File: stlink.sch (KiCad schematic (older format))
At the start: 7 parts, among them U5 STM32F103C(8-B)Tx

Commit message: Continue work at jtag
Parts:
- added C? (x2): 20pF/50V, symbol Capacitors_Smd0603:20pF
- added C?: 100n/50V, symbol Capacitors_Smd0603:100n
- added R? (x2): 10k, symbol Resistors_Smd0603:10k
- added R? (x2): 4k7, symbol Resistors_Smd0603:4k7
- added R?: 100k, symbol Resistors_Smd0603:100k
- added U?: MCP1700T-3302E_MB, symbol Linear_Regulators:MCP1700T-3302E_MB
- added X?: 8.000MHZ, symbol Resonators:ABM3AIG-8.000MHZ-8-1R-T
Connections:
- net GND: now also C?.1, C?.1, C?.2, R?.1, R?.2, R?.2
- net at U5.10 (PA0-WKUP/ADC1_IN0/ADC2_IN0/SYS_WKUP/TIM2_CH1/TIM2_ETR/USART2_CTS): now also R?.2, R?.2
- net at U5.2 (PC13-TAMPER-RTC/RTC_OUT/RTC_TAMPER): now also R?.1
- net at U5.3 (PC14-OSC32_IN/RCC_OSC32_IN): now also R?.1
- net at U5.5 (PD0-OSC_IN/RCC_OSC_IN): now also C?.2, X?.1
- net at U5.6 (PD1-OSC_OUT/RCC_OSC_OUT): now also C?.2, X?.2
- net at U5.7 (NRST): now also C?.1, R?.2
- new net 3V3: R?.1, R?.1
- no-connect marks 0 -> 3

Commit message: Finished work at st-link, figurated elements on pcb
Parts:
- added C26: 1nF/2kV, Capacitors_Smd_1206:1nF_2kV_1206, symbol Capacitors_Smd1206:1nF_2kV_1206
- added C28, C29: 100nF/50V, Capacitors_Smd_0603:100nF_0603, symbol Capacitors_Smd0603:100nF_0603
- added C30: 10uF/6V3, Capacitors_Smd_0805:10uF_0805, symbol Capacitors_Smd0805:10uF_6V3
- added Con4: USB_C_Wurth_632723130112, Connector_USB:USB_C_632723130112, symbol USB_Connectors:USB_C_Wurth_632723130112
- added D2: BAT54C, Diodes:BAT54C, symbol Diodes:BAT54C
- added D3: HSMF-C155, Diodes:HSMF-C155, symbol Diodes:HSMF-C155
- added Q1: BC847B, Transistor_Bipolar:BC847B_SOT23, symbol Transistor_Bipolar:BC847B
- added R10: 10k, Resistor_Smd_0603:10k_0603, symbol Resistors_Smd0603:10k
- added R11: 36k, Resistor_Smd_0603:36k_0603, symbol Resistors_Smd0603:36k
- added R12, R15: 22R, Resistor_Smd_0603:22R_0603, symbol Resistors_Smd0603:22R
- added R13: 1k5, Resistor_Smd_0603:1k5_0603, symbol Resistors_Smd0603:1k5
- added R14, R23: 100R, Resistor_Smd_0603:100R_0603, symbol Resistors_Smd0603:100R
- added R16, R17: 220R, Resistor_Smd_0603:220R_0603, symbol Resistors_Smd0603:220R
- added R21: 100k, Resistor_Smd_0603:100k_0603, symbol Resistors_Smd0603:100k
- added R24: 0R, Resistor_Smd_0603:0R_0603, symbol Resistors_Smd0603:0R
- C27: renamed from C?; footprint (none) -> Capacitors_Smd_0603:100nF_0603
- C31, C32: renamed from C?; footprint (none) -> Capacitors_Smd_0603:20pF_0603
- R18, R20: renamed from R?; footprint (none) -> Resistor_Smd_0603:10k_0603
- R19, R22: renamed from R?; footprint (none) -> Resistor_Smd_0603:4k7_0603
- R9: renamed from R?; footprint (none) -> Resistor_Smd_0603:100k_0603
- U6: renamed from U?; footprint (none) -> Linear:MCP1700T-3302E_MB_SOT89
- X1: renamed from X?; footprint (none) -> Resonators:ABM3AIG-8.000MHZ-8-1R-T
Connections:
- net 3V3: now also C21.1, C22.1, C23.1, C24.1, C25.1, L6.2, U5.1 (VBAT), U5.24 (VDD), U5.36 (VDD), U5.48 (VDD), U6.3 (Vout), C29.1, C30.1, D3.1 (A1), Q1.3 (C)
- net GND: now also U5.20 (PB2), U6.1 (GND), C26.1, C28.2, C29.2, C30.2, Con4.A1 (GND), Con4.A12 (GND_1), Con4.B1 (GND_2), Con4.B12 (GND_3), D3.4 (C2), R11.1, R21.1, R24.1
- net STLINK_TX: now reaches U5.12 (PA2/ADC1_IN2/ADC2_IN2/TIM2_CH3/USART2_TX)
- net STLINK_RX: now reaches U5.13 (PA3/ADC1_IN3/ADC2_IN3/TIM2_CH4/USART2_RX)
- net JTCK: now reaches U5.15 (PA5/ADC1_IN5/ADC2_IN5/SPI1_SCK)
- net JTDO: now reaches U5.16 (PA6/ADC1_IN6/ADC2_IN6/SPI1_MISO/TIM1_BKIN/TIM3_CH1)
- net JTDI: now reaches U5.17 (PA7/ADC1_IN7/ADC2_IN7/SPI1_MOSI/TIM1_CH1N/TIM3_CH2)
- net JTRST: now reaches U5.18 (PB0/ADC1_IN8/ADC2_IN8/TIM1_CH2N/TIM3_CH3)
- net at U5.25 (PB12/I2C2_SMBA/SPI2_NSS/TIM1_BKIN/USART3_CK): now also R23.2
- net STLINK-SWCLK: now reaches U5.26 (PB13/SPI2_SCK/TIM1_CH1N/USART3_CTS)
- net JTMS: now reaches U5.27 (PB14/SPI2_MISO/TIM1_CH2N/USART3_RTS)
- net JTMS: now also R23.1
- net at U5.30 (PA9/TIM1_CH2/USART1_TX): now also R16.2, R17.2
- net STLINK-SWO: now reaches U5.31 (PA10/TIM1_CH3/USART1_RX)
- net at U5.32 (PA11/ADC1_EXTI11/ADC2_EXTI11/CAN_RX/TIM1_CH4/USART1_CTS/USB_DM): now also R12.1
- net at U5.33 (PA12/CAN_TX/TIM1_ETR/USART1_RTS/USB_DP): now also R15.1
- net STM-JTMS-SWDIO: now reaches U5.34 (PA13/SYS_JTMS-SWDIO)
- net STM-JTCK-SWCLK: now reaches U5.37 (PA14/SYS_JTCK-SWCLK)
- net at U5.38 (PA15/ADC1_EXTI15/ADC2_EXTI15/SPI1_NSS/SYS_JTDI/TIM2_CH1/TIM2_ETR): now also R14.2
- net at U5.39 (PB3/SPI1_SCK/SYS_JTDO-TRACESWO/TIM2_CH2): now also R24.2
- net at U5.44 (BOOT0): now also R21.2
- net at U6.2 (Vin): now also C28.1, D2.3 (K)
- new net: D3.2 (C1), R16.1
- new net: D3.3 (A2), R17.1
- new net: Con4.A6 (DP1_P), Con4.B6 (DP2_P), R13.1, R15.2
- new net: Con4.A7 (DN1_M), Con4.B7 (DN2_M), R12.2
- new net: Q1.2 (E), R13.2
- new net: Q1.1 (B), R10.2, R11.2, R14.1
- new net 5V: Con4.A4 (VBUS), Con4.A9 (VBUS_1), Con4.B4 (VBUS_2), Con4.B9 (VBUS_3), D2.2 (A), R10.1
- new net POWER_IN_5V: D2.1 (A)
- new net SHDN: C26.2, Con4.S1 (SHIELD), Con4.S2 (SHIELD), Con4.S3 (SHIELD), Con4.S4 (SHIELD)
- no-connect marks 3 -> 26
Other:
- moved on the sheet: C21, C22, C23, C24, C25, C27, C31, C32, L6, R18, R19, R20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

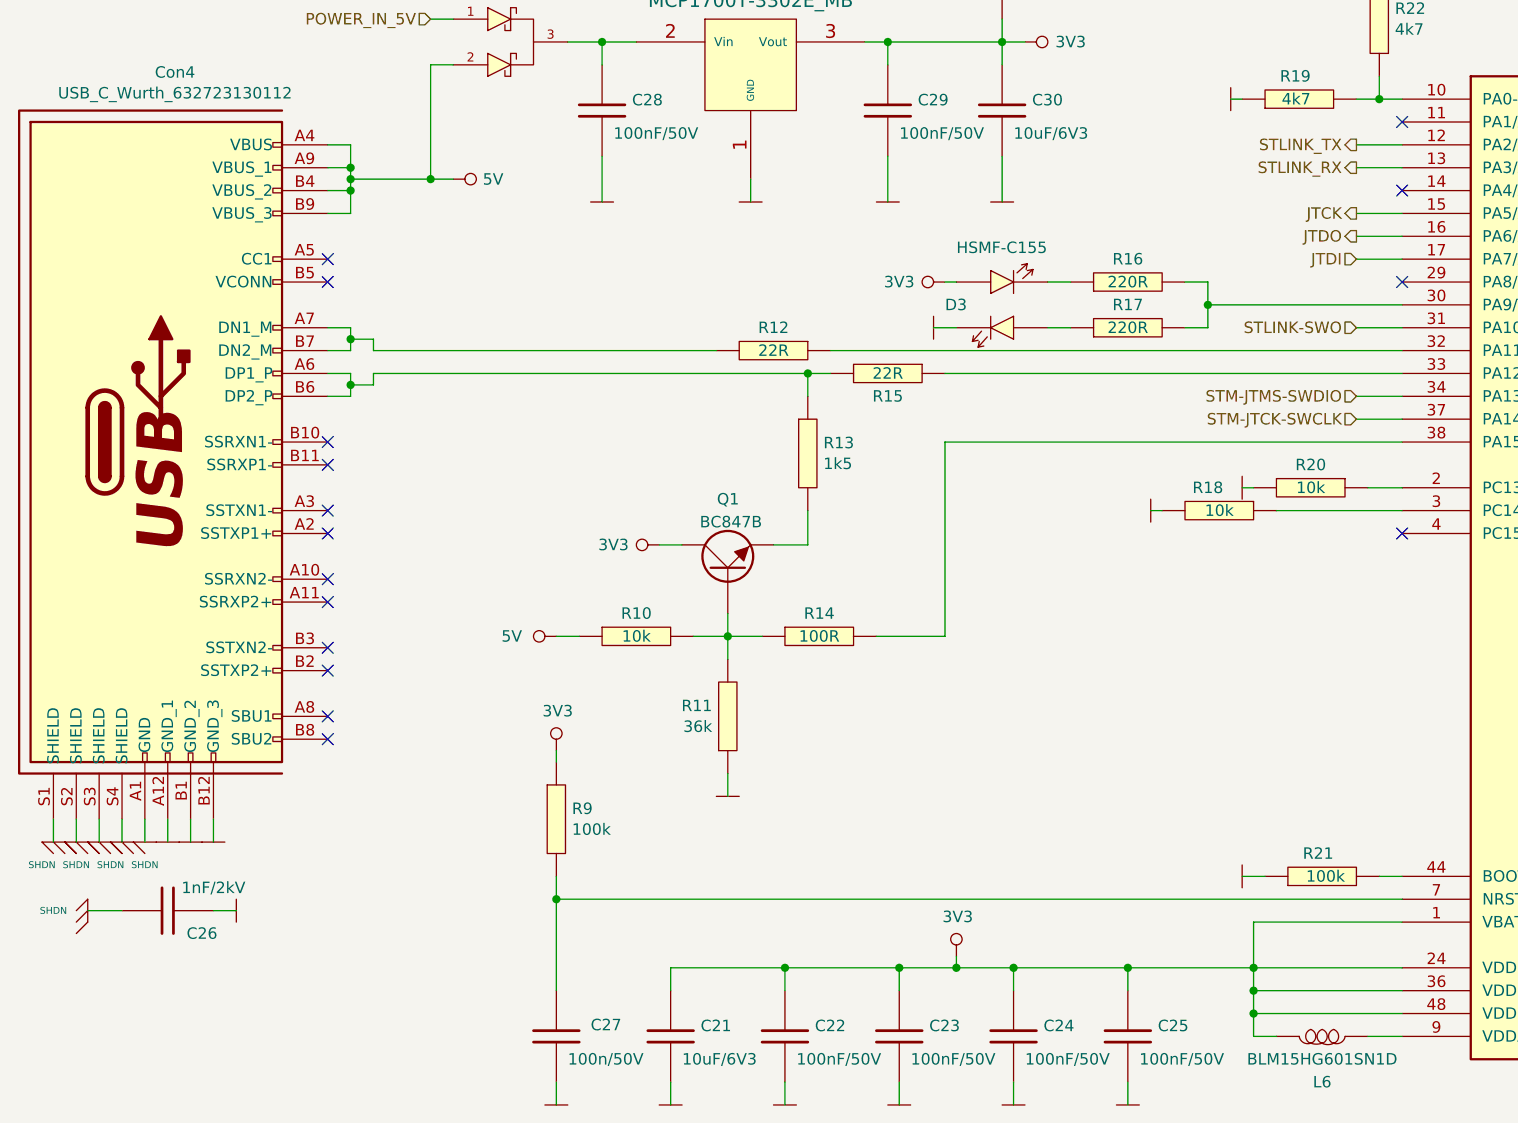
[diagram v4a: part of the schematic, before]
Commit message: Updated schematic, added some components, figurated components on pcb
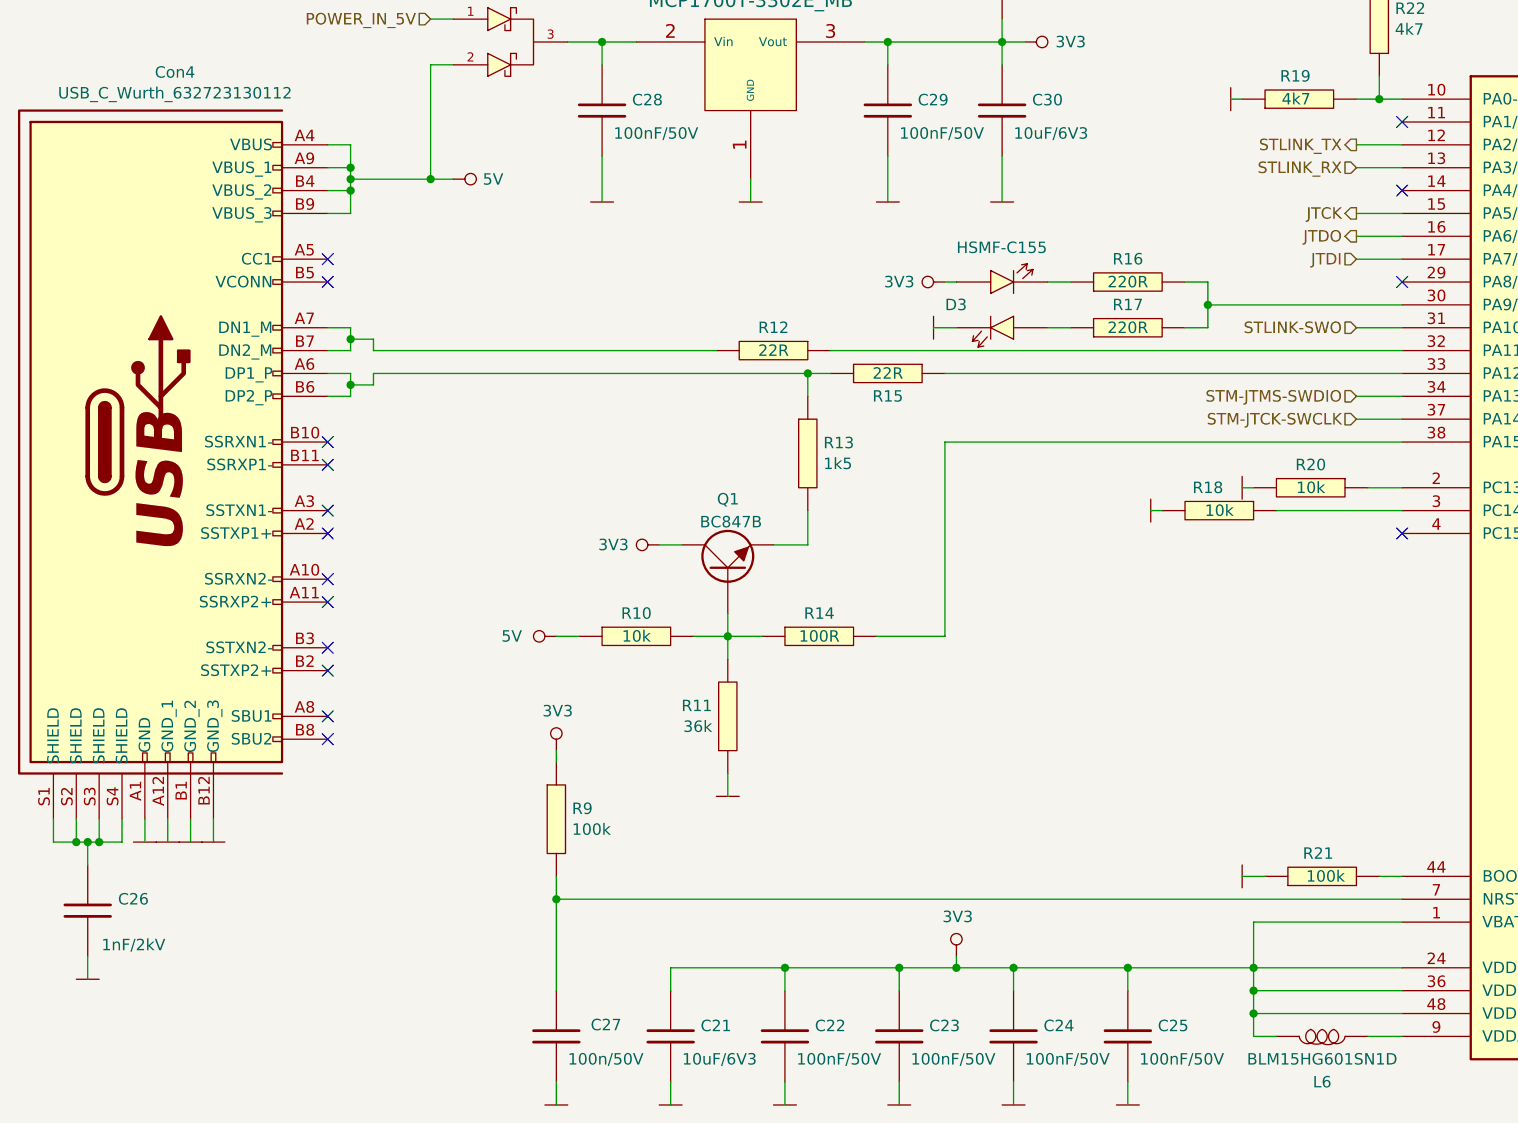
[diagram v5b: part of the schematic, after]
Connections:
- net SHDN: no longer names the net of C26.2, Con4.S1 (SHIELD), Con4.S2 (SHIELD), Con4.S3 (SHIELD), Con4.S4 (SHIELD)
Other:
- moved on the sheet: C26
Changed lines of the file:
@@
 	2500 4700 2600 4700
 Wire Wire Line
-	1450 7050 1600 7050
-$Comp
-L power:SHDN #PWR0135
-U 1 1 600377F0
-P 1450 7050
-F 0 "#PWR0135" H 1570 7060 40  0001 C CNN
-F 1 "SHDN" V 1450 6900 30  0000 C CNN
-F 2 "" H 1450 7050 60  0000 C CNN
-F 3 "" H 1450 7050 60  0000 C CNN
-	1    1450 7050
-	0    1    1    0
-$EndComp
-Wire Wire Line
-	2100 7050 2000 7050
+	1450 7350 1450 7250
 $Comp
 L power:GND_NO_GLOBAL #PWR42
 U 1 1 600350D2
-P 2100 7050
-F 0 "#PWR42" H 2100 7150 30  0001 C CNN
-F 1 "GND_NO_GLOBAL" H 2100 6950 30  0001 C CNN
-F 2 "" H 2100 7050 60  0000 C CNN
-F 3 "" H 2100 7050 60  0000 C CNN
-	1    2100 7050
-	0    1    1    0
+P 1450 7350
+F 0 "#PWR42" H 1450 7450 30  0001 C CNN
+F 1 "GND_NO_GLOBAL" H 1450 7250 30  0001 C CNN
+F 2 "" H 1450 7350 60  0000 C CNN
+F 3 "" H 1450 7350 60  0000 C CNN
+	1    1450 7350
+	-1   0    0    1
 $EndComp
 $Comp
 L Capacitors_Smd1206:1nF_2kV_1206 C26
 U 1 1 60032212
-P 1800 7050
-F 0 "C26" V 1900 7200 50  0000 C CNN
-F 1 "1nF/2kV" V 1700 7250 50  0000 C CNN
-F 2 "Capacitors_Smd_1206:1nF_2kV_1206" H 1600 7150 50  0001 C CNN
-F 3 "Capacitors/Smd_1206/Components_Documentation/1nF_2kV_1206.pdf" H 1600 7150 50  0001 C CNN
-F 4 "YAGEO" H 1800 7050 50  0001 C CNN "Manufacturer"
-F 5 "CC1206KKX7RDBB102" H 1800 7050 50  0001 C CNN "Manufacturer Part Number"
-F 6 "TME" H 1800 7050 50  0001 C CNN "Supplier"
-F 7 "CC1206KKX7RD102" H 1800 7050 50  0001 C CNN "Supplier Part Number"
-F 8 "https://www.tme.eu/pl/details/cc1206kkx7rd102/kondensatory-mlcc-smd-1206/yageo/cc1206kkx7rdbb102/" H 1800 7050 50  0001 C CNN "URL"
-F 9 "0,70900" H 1800 7050 50  0001 C CNN "Price@1pc"
-F 10 "0,15913" H 1800 7050 50  0001 C CNN "Price@1000pcs"
-F 11 "WP" H 1800 7050 50  0001 C CNN "Developer"
-F 12 "1206" H 1800 7050 50  0001 C CNN "Package"
-	1    1800 7050
-	0    1    1    0
-$EndComp
-Wire Wire Line
-	1300 6650 1300 6750
-Wire Wire Line
-	1400 6650 1400 6750
-Wire Wire Line
-	1500 6650 1500 6750
-Wire Wire Line
-	1600 6650 1600 6750
-$Comp
-L power:SHDN #PWR0136
-U 1 1 60024A9F
-P 1300 6750
-F 0 "#PWR0136" H 1420 6760 40  0001 C CNN
-F 1 "SHDN" H 1250 6650 30  0000 C CNN
-F 2 "" H 1300 6750 60  0000 C CNN
-F 3 "" H 1300 6750 60  0000 C CNN
-	1    1300 6750
-	1    0    0    -1
-$EndComp
-$Comp
-L power:SHDN #PWR0137
-U 1 1 600246CB
-P 1400 6750
-F 0 "#PWR0137" H 1520 6760 40  0001 C CNN
-F 1 "SHDN" H 1400 6650 30  0000 C CNN
-F 2 "" H 1400 6750 60  0000 C CNN
-F 3 "" H 1400 6750 60  0000 C CNN
-	1    1400 6750
-	1    0    0    -1
-$EndComp
-$Comp
-L power:SHDN #PWR0138
-U 1 1 60022AD2
-P 1500 6750
-F 0 "#PWR0138" H 1620 6760 40  0001 C CNN
-F 1 "SHDN" H 1550 6650 30  0000 C CNN
-F 2 "" H 1500 6750 60  0000 C CNN
-F 3 "" H 1500 6750 60  0000 C CNN
-	1    1500 6750
-	1    0    0    -1
-$EndComp
-$Comp
-L power:SHDN #PWR0139
-U 1 1 600221FB
-P 1600 6750
-F 0 "#PWR0139" H 1720 6760 40  0001 C CNN
-F 1 "SHDN" H 1700 6650 30  0000 C CNN
-F 2 "" H 1600 6750 60  0000 C CNN
-F 3 "" H 1600 6750 60  0000 C CNN
-	1    1600 6750
-	1    0    0    -1
+P 1450 7050
+F 0 "C26" H 1250 7000 50  0000 C CNN
+F 1 "1nF/2kV" H 1250 7200 50  0000 C CNN
+F 2 "Capacitors_Smd_1206:1nF_2kV_1206" H 1250 7150 50  0001 C CNN
+F 3 "Capacitors/Smd_1206/Components_Documentation/1nF_2kV_1206.pdf" H 1250 7150 50  0001 C CNN
+F 4 "YAGEO" H 1450 7050 50  0001 C CNN "Manufacturer"
+F 5 "CC1206KKX7RDBB102" H 1450 7050 50  0001 C CNN "Manufacturer Part Number"
+F 6 "TME" H 1450 7050 50  0001 C CNN "Supplier"
+F 7 "CC1206KKX7RD102" H 1450 7050 50  0001 C CNN "Supplier Part Number"
+F 8 "https://www.tme.eu/pl/details/cc1206kkx7rd102/kondensatory-mlcc-smd-1206/yageo/cc1206kkx7rdbb102/" H 1450 7050 50  0001 C CNN "URL"
+F 9 "0,70900" H 1450 7050 50  0001 C CNN "Price@1pc"
+F 10 "0,15913" H 1450 7050 50  0001 C CNN "Price@1000pcs"
+F 11 "WP" H 1450 7050 50  0001 C CNN "Developer"
+F 12 "1206" H 1450 7050 50  0001 C CNN "Package"
+	1    1450 7050
+	-1   0    0    1
 $EndComp
 Wire Wire Line
@@
 Wire Wire Line
 	7200 3700 7000 3700
-Text HLabel 7000 3800 0    50   Output ~ 0
+Text HLabel 7000 3800 0    50   Input ~ 0
 STLINK_RX
 Wire Wire Line
@@
 Wire Wire Line
 	14600 4500 14600 4900
+Wire Wire Line
+	1300 6650 1300 6750
+Wire Wire Line
+	1300 6750 1400 6750
+Wire Wire Line
+	1600 6750 1600 6650
+Wire Wire Line
+	1500 6650 1500 6750
+Connection ~ 1500 6750
+Wire Wire Line
+	1500 6750 1600 6750
+Wire Wire Line
+	1400 6650 1400 6750
+Connection ~ 1400 6750
+Wire Wire Line
+	1400 6750 1450 6750
+Wire Wire Line
+	1450 6850 1450 6750
+Connection ~ 1450 6750
+Wire Wire Line
+	1450 6750 1500 6750
 $EndSCHEMATC
